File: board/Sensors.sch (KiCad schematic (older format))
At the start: 8 parts, among them Q1 Phototrans, Q2 Q_NPN_BEC, U1 74HC393

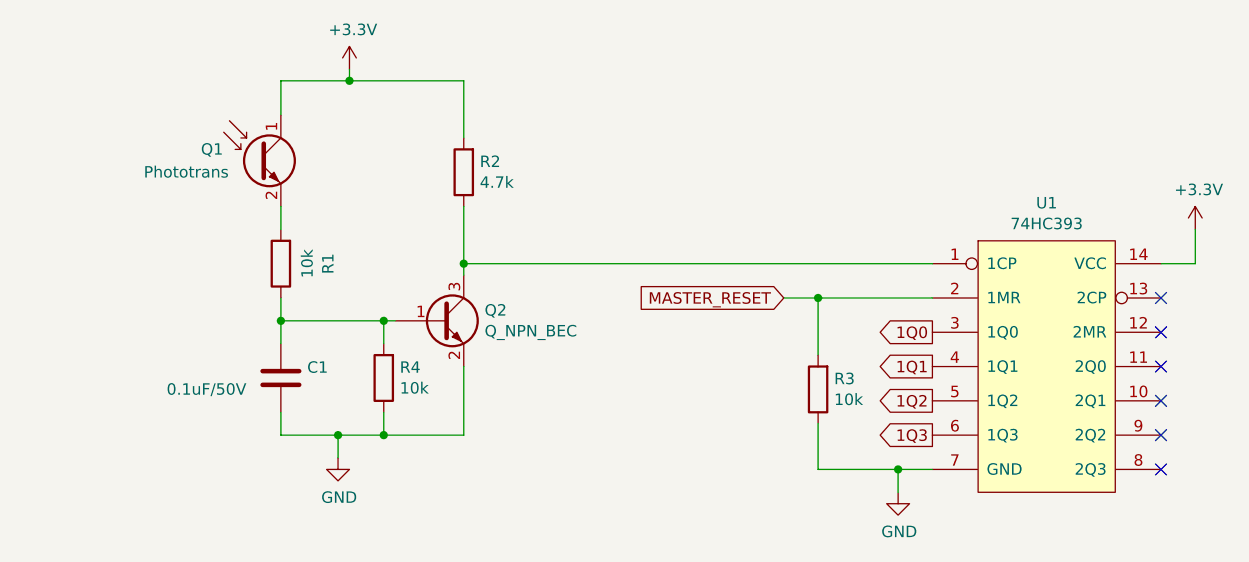
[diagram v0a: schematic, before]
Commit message: Reworked input circuit (again). Added binary counter bypass.
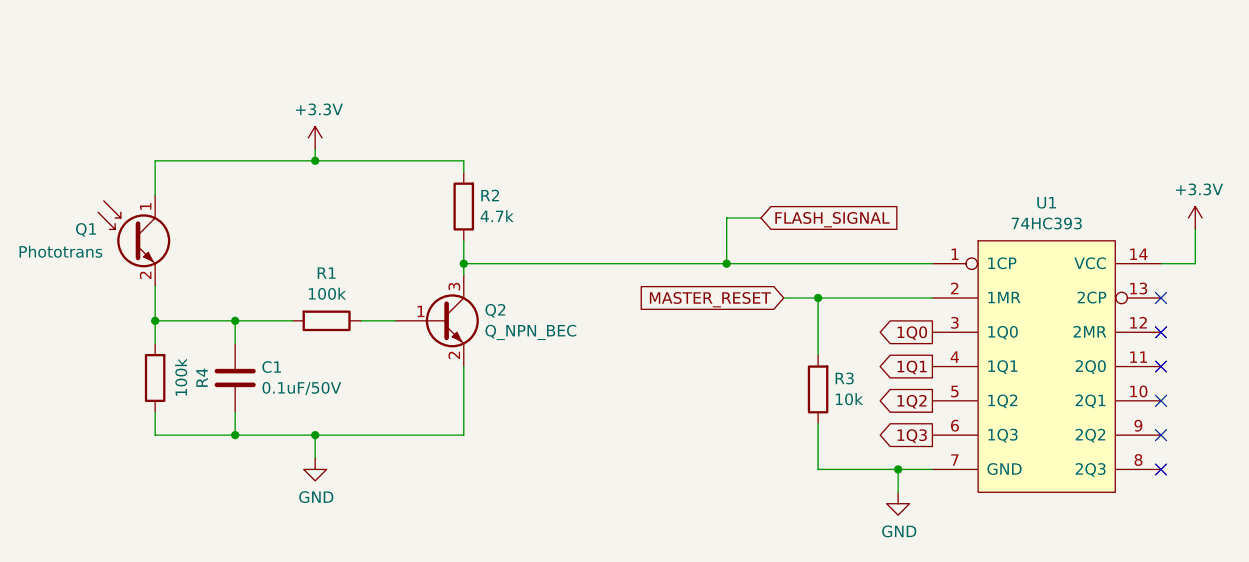
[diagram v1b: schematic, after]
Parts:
- R1, R4: value 10k -> 100k
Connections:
- net at Q2.1 (B), R1.1: no longer C1.1, R4.2
- net FLASH_SIGNAL: now reaches Q2.3 (C), R2.1, U1.1 (1CP)
- net at Q1.2 (E), R1.2: now also C1.1, R4.2
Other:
- moved on the sheet: C1, Q1, R1, R2
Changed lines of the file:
@@
 EESchema Schematic File Version 4
 LIBS:power_stalker_esp-cache
-EELAYER 29 0
+EELAYER 30 0
 EELAYER END
 $Descr A4 11693 8268
@@
 L power:GND #PWR09
 U 1 1 5BE94315
-P 4250 4050
-F 0 "#PWR09" H 4250 3800 50  0001 C CNN
-F 1 "GND" H 4255 3877 50  0000 C CNN
-F 2 "" H 4250 4050 50  0001 C CNN
-F 3 "" H 4250 4050 50  0001 C CNN
-	1    4250 4050
+P 4150 4050
+F 0 "#PWR09" H 4150 3800 50  0001 C CNN
+F 1 "GND" H 4155 3877 50  0000 C CNN
+F 2 "" H 4150 4050 50  0001 C CNN
+F 3 "" H 4150 4050 50  0001 C CNN
+	1    4150 4050
 	1    0    0    -1
 $EndComp
@@
 L Device:C C1
 U 1 1 5BE943F3
-P 4000 3700
-F 0 "C1" H 4115 3746 50  0000 L CNN
-F 1 "0.1uF/50V" H 3500 3650 50  0000 L CNN
-F 2 "Capacitor_SMD:C_0603_1608Metric_Pad1.05x0.95mm_HandSolder" H 4038 3550 50  0001 C CNN
-F 3 "~" H 4000 3700 50  0001 C CNN
-	1    4000 3700
+P 3800 3700
+F 0 "C1" H 3915 3746 50  0000 L CNN
+F 1 "0.1uF/50V" H 3915 3655 50  0000 L CNN
+F 2 "Capacitor_SMD:C_0603_1608Metric_Pad1.05x0.95mm_HandSolder" H 3838 3550 50  0001 C CNN
+F 3 "~" H 3800 3700 50  0001 C CNN
+	1    3800 3700
 	1    0    0    -1
 $EndComp
@@
 L Device:R R1
 U 1 1 5BE944CC
-P 4000 3200
-F 0 "R1" V 3793 3200 50  0000 C CNN
-F 1 "10k" V 3884 3200 50  0000 C CNN
-F 2 "Resistor_SMD:R_0603_1608Metric_Pad1.05x0.95mm_HandSolder" V 3930 3200 50  0001 C CNN
-F 3 "~" H 4000 3200 50  0001 C CNN
-	1    4000 3200
-	-1   0    0    1
+P 4200 3450
+F 0 "R1" V 3993 3450 50  0000 C CNN
+F 1 "100k" V 4084 3450 50  0000 C CNN
+F 2 "Resistor_SMD:R_0603_1608Metric_Pad1.05x0.95mm_HandSolder" V 4130 3450 50  0001 C CNN
+F 3 "~" H 4200 3450 50  0001 C CNN
+	1    4200 3450
+	0    1    1    0
 $EndComp
 $Comp
 L Device:R R2
 U 1 1 5BE94578
-P 4800 2800
-F 0 "R2" H 4730 2754 50  0000 R CNN
-F 1 "4.7k" H 4730 2845 50  0000 R CNN
-F 2 "Resistor_SMD:R_0603_1608Metric_Pad1.05x0.95mm_HandSolder" V 4730 2800 50  0001 C CNN
-F 3 "~" H 4800 2800 50  0001 C CNN
-	1    4800 2800
+P 4800 2950
+F 0 "R2" H 4730 2904 50  0000 R CNN
+F 1 "4.7k" H 4730 2995 50  0000 R CNN
+F 2 "Resistor_SMD:R_0603_1608Metric_Pad1.05x0.95mm_HandSolder" V 4730 2950 50  0001 C CNN
+F 3 "~" H 4800 2950 50  0001 C CNN
+	1    4800 2950
 	-1   0    0    1
 $EndComp
 Wire Wire Line
-	4800 2650 4800 2400
+	4800 2800 4800 2750
 $Comp
 L power:+3.3V #PWR08
 U 1 1 5BE94675
-P 4300 2350
-F 0 "#PWR08" H 4300 2200 50  0001 C CNN
-F 1 "+3.3V" H 4315 2523 50  0000 C CNN
-F 2 "" H 4300 2350 50  0001 C CNN
-F 3 "" H 4300 2350 50  0001 C CNN
-	1    4300 2350
+P 4150 2700
+F 0 "#PWR08" H 4150 2550 50  0001 C CNN
+F 1 "+3.3V" H 4165 2873 50  0000 C CNN
+F 2 "" H 4150 2700 50  0001 C CNN
+F 3 "" H 4150 2700 50  0001 C CNN
+	1    4150 2700
 	1    0    0    -1
 $EndComp
@@
 F 1 "74HC393" H 7350 5374 50  0000 C CNN
 F 2 "Package_SO:SOIC-14_3.9x8.7mm_P1.27mm" H 7350 4450 50  0001 C CNN
-F 3 "https://assets.nexperia.com/documents/data-sheet/74HC_HCT393.pdf" H 7350 4450 50  0001 C CNN
+F 3 "" H 7350 4450 50  0001 C CNN
 F 4 "1085344" H 7350 4200 50  0001 C CNN "Farnell"
 F 5 "74HC393D" H 7350 4200 50  0001 C CNN "Ref"
@@
 	4800 3650 4800 3950
 Wire Wire Line
-	4250 3950 4450 3950
+	4050 3450 3800 3450
+Wire Wire Line
+	3450 3450 3450 3550
+Wire Wire Line
+	3450 3850 3450 3950
+Wire Wire Line
+	3450 3950 3800 3950
+Wire Wire Line
+	4350 3450 4500 3450
+Wire Wire Line
+	3450 2750 4150 2750
+Wire Wire Line
+	4150 4050 4150 3950
+Wire Wire Line
+	4150 3950 4800 3950
+Wire Wire Line
+	4150 2700 4150 2750
+Wire Wire Line
+	4150 2750 4800 2750
 $Comp
 L Device:Q_Photo_NPN Q1
 U 1 1 5BE97372
-P 3900 2750
-F 0 "Q1" H 3650 2800 50  0000 L CNN
-F 1 "Phototrans" H 3400 2700 50  0000 L CNN
-F 2 "w_conn_mpt:mpt_0,5-2-2,54" H 4100 2850 50  0001 C CNN
-F 3 "~" H 3900 2750 50  0001 C CNN
-F 4 "1497675" H 3900 2750 50  0001 C CNN "Farnell"
-F 5 "TEPT4400" H 3900 2750 50  0001 C CNN "Ref"
-	1    3900 2750
-	1    0    0    -1
-$EndComp
-Wire Wire Line
-	4000 2400 4000 2550
-Wire Wire Line
-	4800 2950 4800 3200
-Wire Wire Line
-	4800 3200 6850 3200
+P 3350 3100
+F 0 "Q1" H 3100 3150 50  0000 L CNN
+F 1 "Phototrans" H 2850 3050 50  0000 L CNN
+F 2 "w_conn_mpt:mpt_0,5-2-2,54" H 3550 3200 50  0001 C CNN
+F 3 "~" H 3350 3100 50  0001 C CNN
+F 4 "1497675" H 3350 3100 50  0001 C CNN "Farnell"
+F 5 "TEPT4400" H 3350 3100 50  0001 C CNN "Ref"
+	1    3350 3100
+	1    0    0    -1
+$EndComp
+Wire Wire Line
+	3450 2750 3450 2900
+Wire Wire Line
+	3450 3300 3450 3450
+Connection ~ 3450 3450
+Wire Wire Line
+	4800 3100 4800 3200
+Wire Wire Line
+	4800 3200 5950 3200
+Connection ~ 4800 3200
 Wire Wire Line
 	4800 3200 4800 3250
@@
 $Comp
 L Device:R R4
-U 1 1 5D192C7B
-P 4450 3700
-F 0 "R4" H 4380 3654 50  0000 R CNN
-F 1 "10k" H 4380 3745 50  0000 R CNN
-F 2 "Resistor_SMD:R_0603_1608Metric_Pad1.05x0.95mm_HandSolder" V 4380 3700 50  0001 C CNN
-F 3 "~" H 4450 3700 50  0001 C CNN
-	1    4450 3700
+U 1 1 5E99ECC7
+P 3450 3700
+F 0 "R4" V 3243 3700 50  0000 C CNN
+F 1 "100k" V 3334 3700 50  0000 C CNN
+F 2 "Resistor_SMD:R_0603_1608Metric_Pad1.05x0.95mm_HandSolder" V 3380 3700 50  0001 C CNN
+F 3 "~" H 3450 3700 50  0001 C CNN
+	1    3450 3700
 	-1   0    0    1
 $EndComp
-Wire Wire Line
-	4250 3950 4250 4050
-Connection ~ 4250 3950
-Wire Wire Line
-	4450 3450 4450 3550
-Wire Wire Line
-	4450 3850 4450 3950
-Wire Wire Line
-	4300 2400 4800 2400
-Wire Wire Line
-	4300 2350 4300 2400
-Connection ~ 4300 2400
-Wire Wire Line
-	4450 3450 4500 3450
-Connection ~ 4450 3950
-Wire Wire Line
-	4450 3950 4800 3950
-Wire Wire Line
-	4000 3950 4250 3950
-Wire Wire Line
-	4000 2400 4300 2400
-Wire Wire Line
-	4000 2950 4000 3050
-Wire Wire Line
-	4000 3350 4000 3450
-Wire Wire Line
-	4000 3950 4000 3850
-Wire Wire Line
-	4450 3450 4000 3450
-Connection ~ 4450 3450
-Connection ~ 4000 3450
-Wire Wire Line
-	4000 3450 4000 3550
-Connection ~ 4800 3200
+Connection ~ 4150 2750
+Connection ~ 4150 3950
+Wire Wire Line
+	3800 3550 3800 3450
+Connection ~ 3800 3450
+Wire Wire Line
+	3800 3450 3450 3450
+Wire Wire Line
+	3800 3850 3800 3950
+Connection ~ 3800 3950
+Wire Wire Line
+	3800 3950 4150 3950
+Text GLabel 6100 3000 2    50   Input ~ 0
+FLASH_SIGNAL
+Wire Wire Line
+	5950 3000 5950 3200
+Connection ~ 5950 3200
+Wire Wire Line
+	5950 3200 6850 3200
+Wire Wire Line
+	5950 3000 6100 3000
 $EndSCHEMATC
